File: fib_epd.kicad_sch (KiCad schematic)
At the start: 53 parts, among them U1 TPS651851RSLT, U1101 ESP32-S3-WROOM-1U

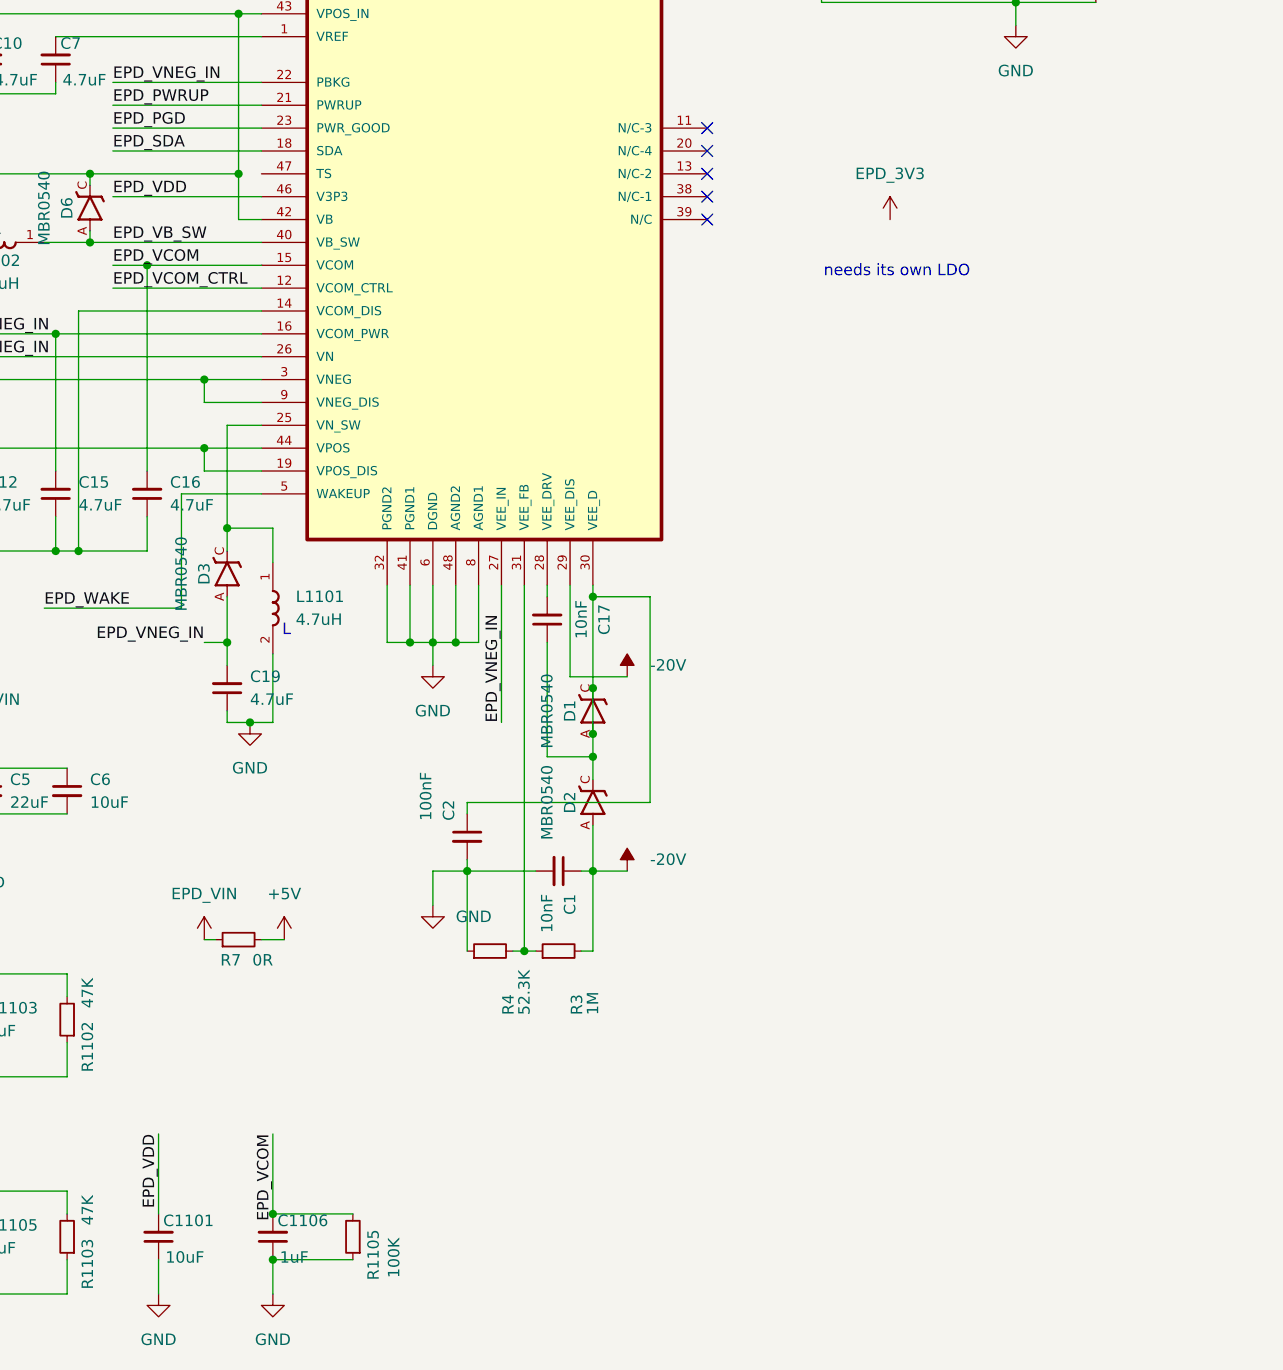
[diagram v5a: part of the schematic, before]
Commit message: refactored PCIe pages
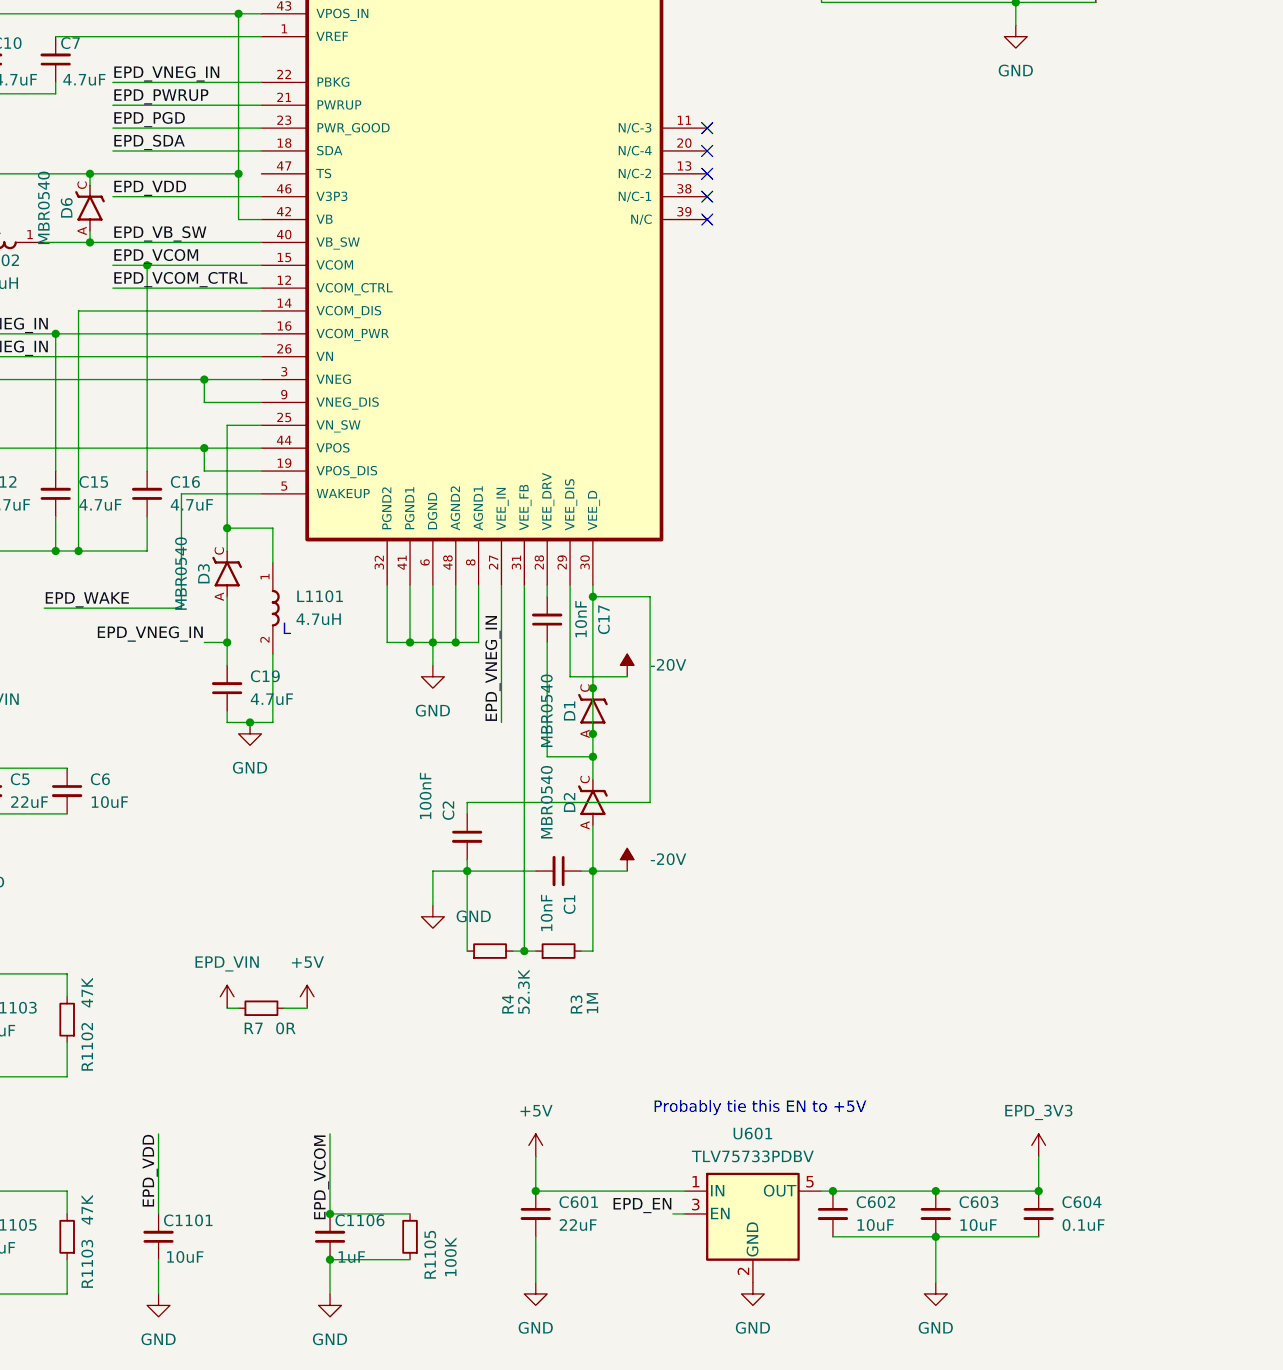
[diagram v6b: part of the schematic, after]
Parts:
- added C601: 22uF, Capacitor_SMD:C_0805_2012Metric, symbol Device:C_Small
- added C602, C603: 10uF, Capacitor_SMD:C_0603_1608Metric, symbol Device:C_Small
- added C604: 0.1uF, Capacitor_SMD:C_0603_1608Metric, symbol Device:C_Small
- added U601: TLV75733PDBV, Package_TO_SOT_SMD:SOT-23-5, symbol Regulator_Linear:TLV75733PDBV
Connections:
- net +5V: now also C601.1, U601.1 (IN)
- net EPD_3V3: now also C602.1, C603.1, C604.1, U601.5 (OUT)
- net GND: now also C601.2, C602.2, C603.2, C604.2, U601.2 (GND)
- new net EPD_EN: U601.3 (EN)
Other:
- note added: "Probably tie this EN to +5V"
- note removed: "needs its own LDO"
- moved on the sheet: C1106, R1105, R7

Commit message: added some missing footprints, stared working ono power-on and sequencing
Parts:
- D1, D2, D3, D4, D5, D6: footprint MBR0540:SOD-123 -> Fibel2:SOD-123
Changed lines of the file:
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@@
 			)
 		)
-		(property "Footprint" "MBR0540:SOD-123"
+		(property "Footprint" "Fibel2:SOD-123"
 			(at 107.188 132.08 0)
 			(effects
@@
 			)
 		)
-		(property "Footprint" "MBR0540:SOD-123"
+		(property "Footprint" "Fibel2:SOD-123"
 			(at 151.13 24.638 0)
 			(effects
@@
 			)
 		)
-		(property "Footprint" "MBR0540:SOD-123"
+		(property "Footprint" "Fibel2:SOD-123"
 			(at 140.97 24.638 0)
 			(effects
@@
 			)
 		)
-		(property "Footprint" "MBR0540:SOD-123"
+		(property "Footprint" "Fibel2:SOD-123"
 			(at 66.548 106.68 0)
 			(effects
@@
 			)
 		)
-		(property "Footprint" "MBR0540:SOD-123"
+		(property "Footprint" "Fibel2:SOD-123"
 			(at 51.308 66.04 0)
 			(effects
@@
 			)
 		)
-		(property "Footprint" "MBR0540:SOD-123"
+		(property "Footprint" "Fibel2:SOD-123"
 			(at 107.188 121.92 0)
 			(effects
